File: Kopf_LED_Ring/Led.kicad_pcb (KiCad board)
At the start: 2 copper layers, 28 x 28 mm, 60 parts, among them IC1 AL8808, IC2 AL8808, IC3 AL8808, P1 CONN_01X04, Q1 Q_NMOS_GSD

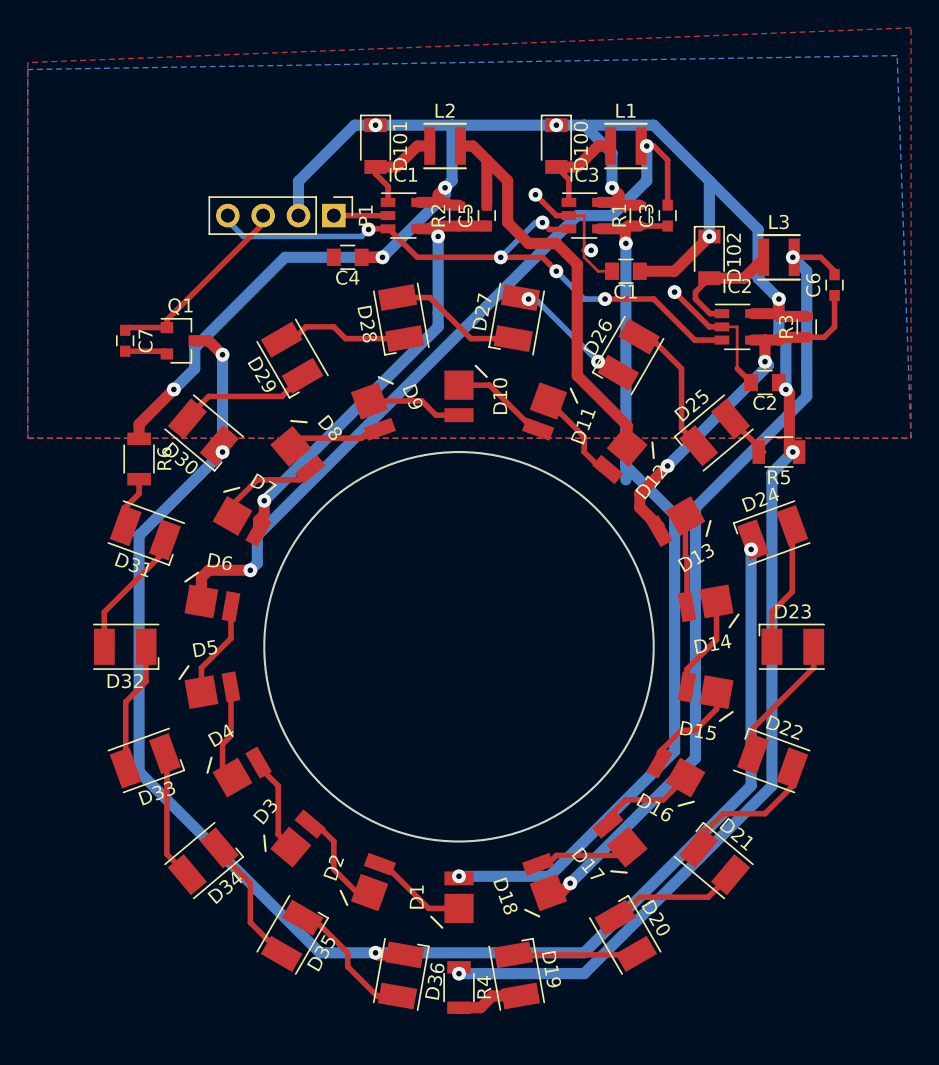
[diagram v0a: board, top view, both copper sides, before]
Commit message: Temperatursensor hinzugefügt
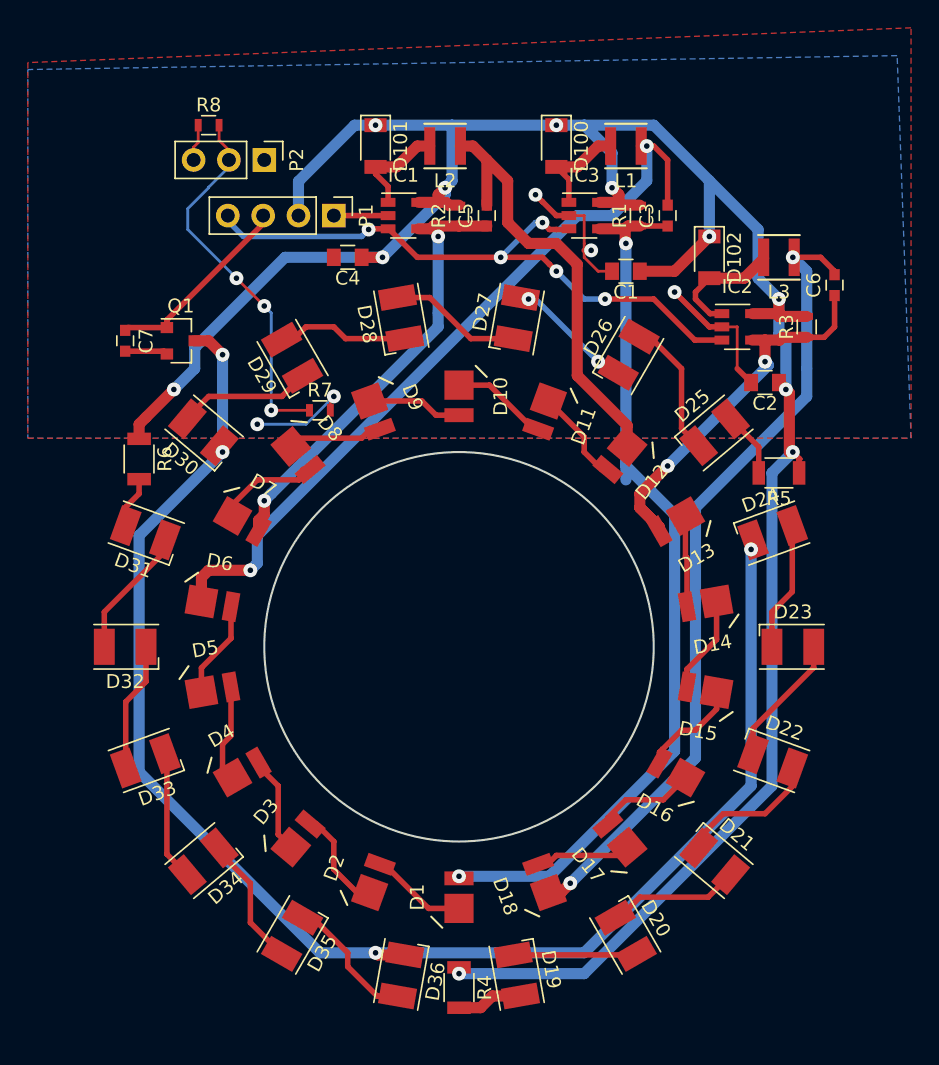
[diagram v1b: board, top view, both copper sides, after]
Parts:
- added P2: CONN_01X03, Socket_Strips:Socket_Strip_Straight_1x03_Pitch2.54mm, F.Cu at (47.0, 29.0)
- added R7: TempSens, Resistors_SMD:R_0603, F.Cu at (51.0, 47.0)
- added R8: R, Resistors_SMD:R_0603, F.Cu at (43.0, 26.5)
- moved R5 1.50 mm to (84.0, 51.5)
- turned L1 to 180 degrees
- turned L2 to 180 degrees
- turned L3 to 180 degrees
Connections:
- L1 pad 1: /SW1 -> /L1
- L1 pad 2: /L1 -> /SW1
- L2 pad 1: /SW2 -> /L2
- L2 pad 2: /L2 -> /SW2
- L3 pad 1: /SW3 -> /L3
- L3 pad 2: /L3 -> /SW3
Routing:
- net /TempSens: track 0.00 -> 27.3 mm, vias 0 -> 3
- net GND: track 27.0 -> 34.4 mm, vias 3 -> 5
- net /TempSensH: track 0.00 -> 3.14 mm
- net +24V: track 178.6 -> 180.4 mm
- net Net-(D25-Pad2): track 3.37 -> 4.72 mm

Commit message: EdgCuts gezeichnet
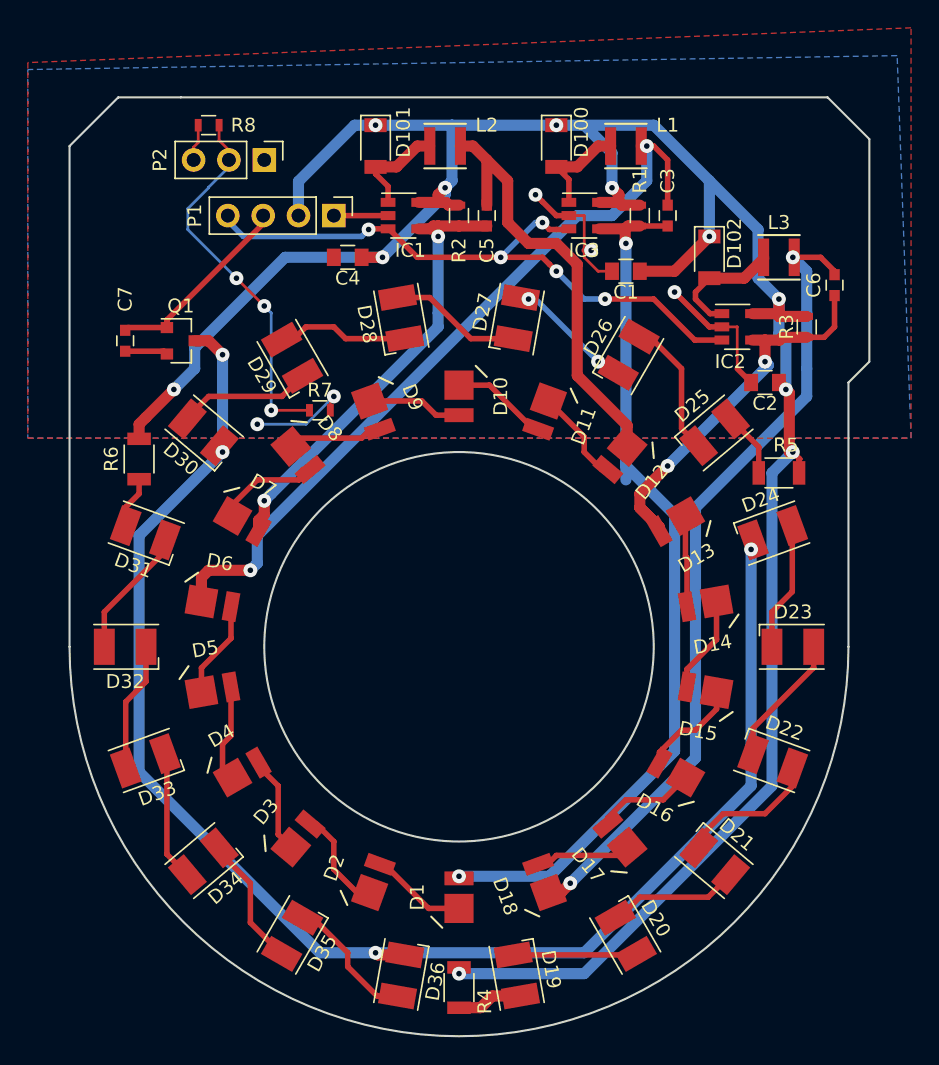
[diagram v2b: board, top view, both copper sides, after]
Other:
- board size 28 x 28 mm -> 57.5 x 67.5 mm
